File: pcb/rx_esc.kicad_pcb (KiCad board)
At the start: 2 copper layers, 54 parts, among them CON1 AVR-ISP-6, J1 CONN_01X02, J2 CONN_01X02, J3 CONN_02X06, J4 CONN_01X03, J5 CONN_01X03, J6 CONN_01X02, J7 CONN_01X02, Q1 Q_NMOS_DGS, Q2 Q_NMOS_DGS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

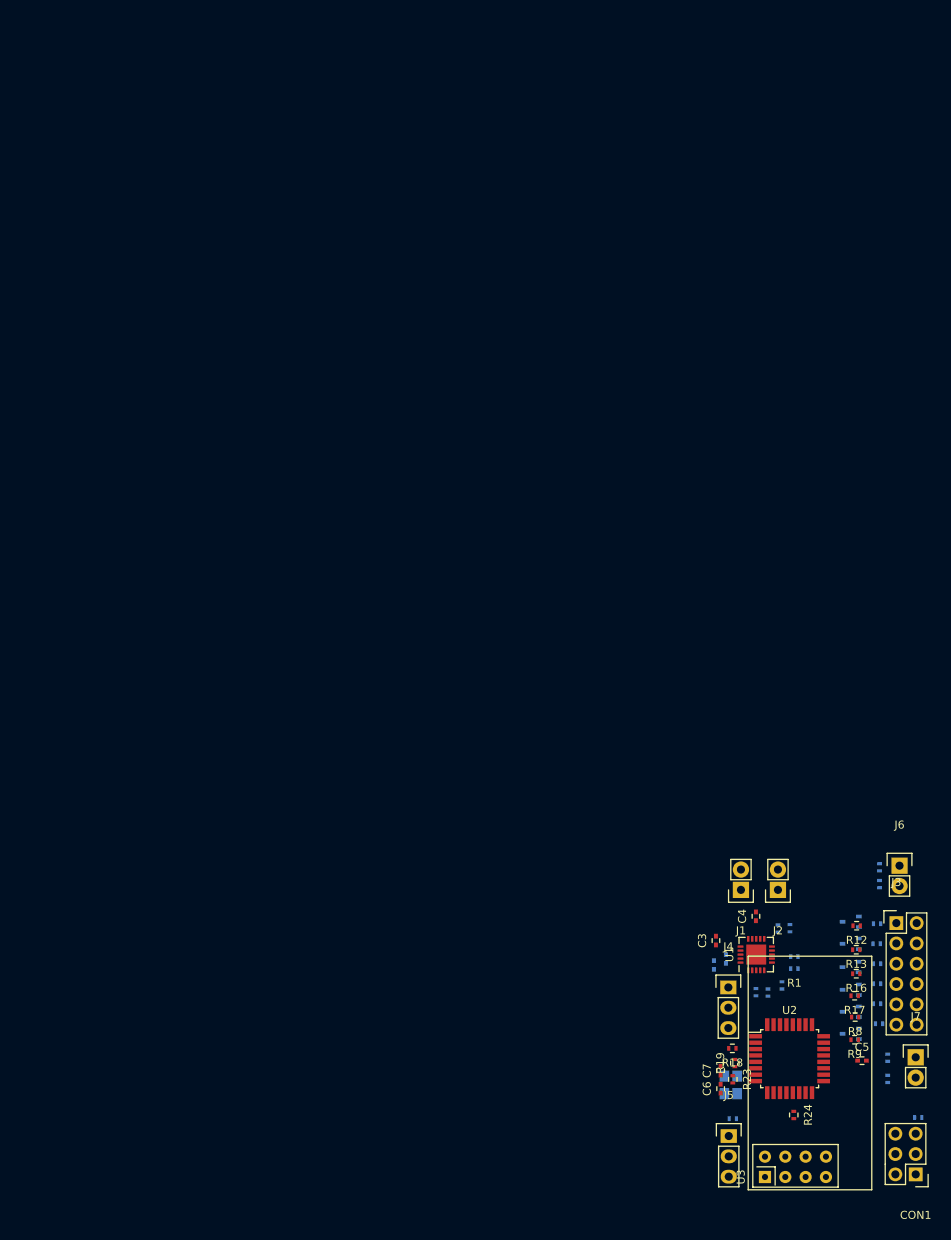
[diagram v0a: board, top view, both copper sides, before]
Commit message: VE 24-12-17 Add power supply
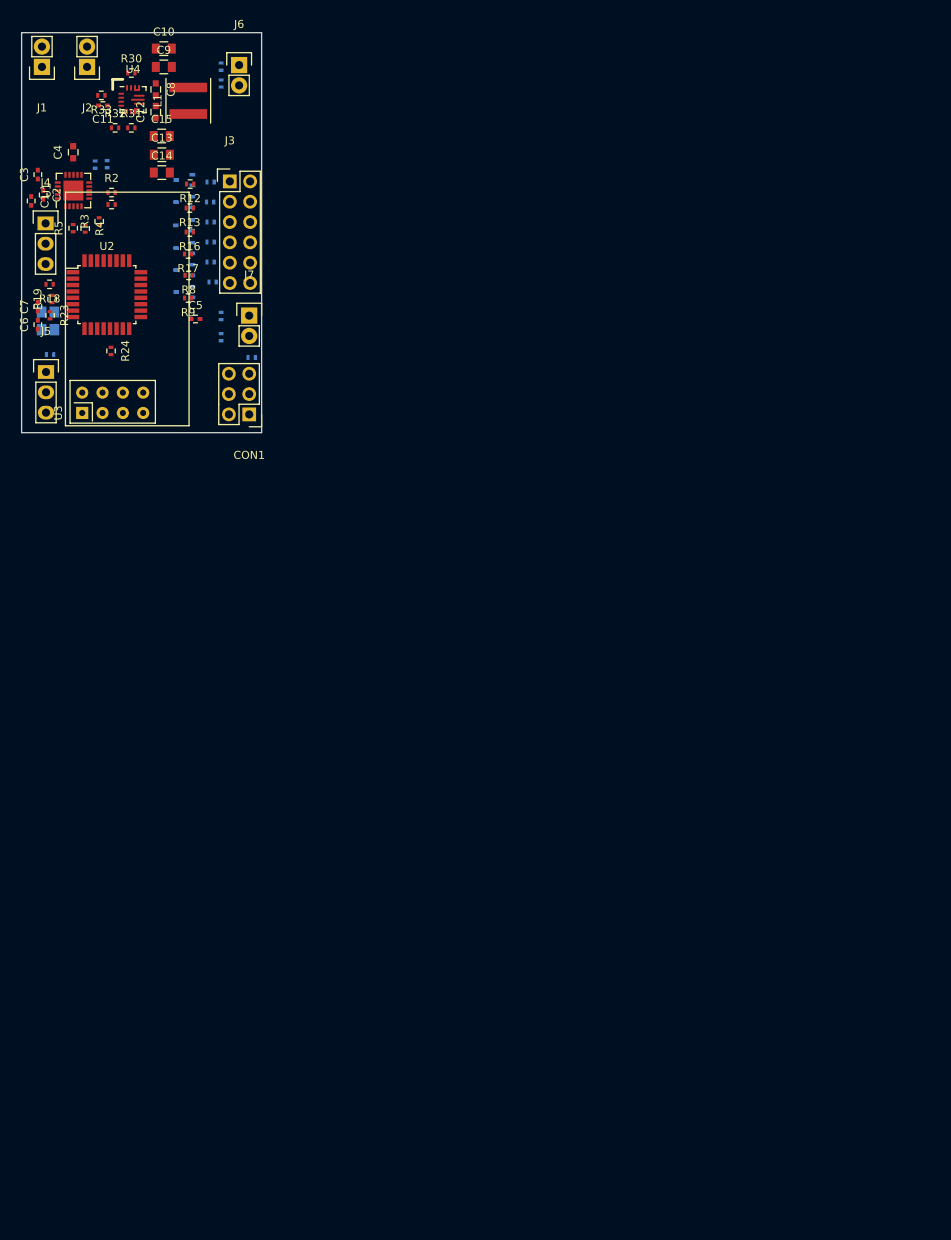
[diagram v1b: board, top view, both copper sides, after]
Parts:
- added C10: 10uf, Capacitors_SMD:C_0805, F.Cu at (17.8, -48.0)
- added C11: 100nF, Capacitors_SMD:C_0402, F.Cu at (10.2, -40.9)
- added C12: 10uf, Capacitors_SMD:C_0603, F.Cu at (16.8, -40.1)
- added C13: 10uf, Capacitors_SMD:C_0805, F.Cu at (17.5, -34.7)
- added C14: 10uf, Capacitors_SMD:C_0805, F.Cu at (17.5, -32.5)
- added C15: 10uf, Capacitors_SMD:C_0805, F.Cu at (17.5, -37.1)
- added C8: 10uf, Capacitors_SMD:C_0603, F.Cu at (16.8, -42.9)
- added C9: 10uf, Capacitors_SMD:C_0805, F.Cu at (17.8, -45.7)
- added L1: 1.5uH, Inductors_SMD:L_Coilcraft_XAL5030, F.Cu at (20.8, -41.5)
- added R30: 10k, Resistors_SMD:R_0402, F.Cu at (13.7, -45.0)
- added R31: 150k, Resistors_SMD:R_0402, F.Cu at (13.7, -38.1)
- added R32: 470k, Resistors_SMD:R_0402, F.Cu at (11.7, -38.1)
- added R33: 100k, Resistors_SMD:R_0402, F.Cu at (9.96, -42.2)
- added U4: TPS63070, FOOTPRINT:QFN-16-1EP_3x3mm_Pitch0.5mm, F.Cu at (13.9, -41.6)
- C1, C2, R1, R2, R3, R4, R5: moved to F.Cu
- C4: footprint Capacitors_SMD:C_0402 -> Capacitors_SMD:C_0603
- moved J1 135.0 mm to (2.54, -45.7)
- moved J2 134.3 mm to (8.18, -45.7)
- moved J6 129.7 mm to (27.2, -46.0)
- moved R28 129.6 mm to (24.9, -45.8)
- moved R29 129.6 mm to (24.9, -43.6)
- moved C1 128.1 mm to (1.20, -29.0)
- moved C2 128.1 mm to (2.70, -29.7)
- moved C4 128.1 mm to (6.45, -35.1)
- moved C6 128.1 mm to (2.03, -13.5)
- moved C7 128.1 mm to (2.03, -15.7)
- moved J4 128.1 mm to (3.00, -26.2)
- moved J5 128.1 mm to (3.05, -7.58)
- moved R1 128.1 mm to (11.2, -28.5)
- moved R18 128.1 mm to (3.50, -18.5)
- moved R19 128.1 mm to (3.81, -16.7)
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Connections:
- net Net-(C1-Pad1) renamed /CP1
- net Net-(C1-Pad2) renamed /CP2
- net Net-(C2-Pad1) renamed /CP3
- net Net-(C2-Pad2) renamed /CP4
- net Net-(C3-Pad1) renamed /VCP
- net Net-(C5-Pad1) renamed /AREF
- net Net-(J4-Pad1) renamed /SERVO1_OUT
- net Net-(J5-Pad1) renamed /SERVO2_OUT
- net Net-(J7-Pad1) renamed /AN
- net Net-(Q1-Pad1) renamed /OUT5_
- net Net-(Q1-Pad2) renamed /PD5_
- net Net-(Q2-Pad1) renamed /OUT6_
- net Net-(Q2-Pad2) renamed /PD6_
- net Net-(Q3-Pad1) renamed /OUT1_
- net Net-(Q3-Pad2) renamed /PC2_
- net Net-(Q4-Pad1) renamed /OUT2_
- net Net-(Q4-Pad2) renamed /PC3_
- net Net-(Q5-Pad1) renamed /OUT3_
- net Net-(Q5-Pad2) renamed /PC4_
- net Net-(Q6-Pad1) renamed /OUT4_
- net Net-(Q6-Pad2) renamed /PC5_
- net Net-(R1-Pad1) renamed /IN3_
- net Net-(R18-Pad1) renamed /PE0
- net Net-(R19-Pad1) renamed /PE1
- net Net-(R2-Pad1) renamed /IN4_
- net Net-(R5-Pad1) renamed /SLP
- net Net-(R6-Pad1) renamed /FL1
- net Net-(R7-Pad1) renamed /FL2
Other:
- board outline added: 30 x 50 mm

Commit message: VE 25-12-17 PCB routed schematic updated
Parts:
- C1, C2: footprint Capacitors_SMD:C_0402 -> Capacitors_SMD:C_0603
- Q1, Q2, Q3, Q4, Q5, Q6: value Q_NMOS_DGS -> MMBT2222
- R1, R2, R3, R4: footprint Resistors_SMD:R_0402 -> Resistors_SMD:R_0603
- R25, R26, R27: moved to F.Cu
- moved R25 8.94 mm to (12.5, -9.59), turned to 270 degrees
- moved J6 1.37 mm to (27.2, -44.6)
- moved R28 1.37 mm to (24.9, -44.4)
- moved R29 1.37 mm to (24.9, -42.3)
- moved J2 1.33 mm to (7.47, -44.6)
- moved C15 1.14 mm to (16.5, -36.6)
- moved C14 1.14 mm to (16.5, -32.0)
- moved C13 1.14 mm to (16.5, -34.2)
- moved J1 1.12 mm to (2.64, -44.6)
- moved R3 1.07 mm to (8.64, -26.3), turned to 180 degrees
- moved C10 1.05 mm to (16.8, -47.8)
- moved C9 1.02 mm to (16.8, -45.7)
- moved R4 0.96 mm to (8.64, -24.8), turned to 180 degrees
- moved R24 0.63 mm to (11.1, -9.60)
- turned R5 to 270 degrees
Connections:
- Q1 pad 1: /OUT5_ -> /PD4_
- Q1 pad 2: /PD5_ -> GND
- Q1 pad 3: GND -> /OUT5_
- Q2 pad 1: /OUT6_ -> /PD6_
- Q2 pad 2: /PD6_ -> GND
- Q2 pad 3: GND -> /OUT6_
- Q3 pad 1: /OUT1_ -> /PC5_
- Q3 pad 2: /PC2_ -> GND
- Q3 pad 3: GND -> /OUT1_
- Q4 pad 1: /OUT2_ -> /PC4_
- Q4 pad 2: /PC3_ -> GND
- Q4 pad 3: GND -> /OUT2_
- Q5 pad 1: /OUT3_ -> /PC3_
- Q5 pad 2: /PC4_ -> GND
- Q5 pad 3: GND -> /OUT3_
- Q6 pad 1: /OUT4_ -> /PC2_
- Q6 pad 2: /PC5_ -> GND
- Q6 pad 3: GND -> /OUT4_
- R12 pad 1: /PC2_ -> /PC5_
- R12 pad 2: /PC2 -> /PC5
- R13 pad 1: /PC3_ -> /PC4_
- R13 pad 2: /PC3 -> /PC4
- R16 pad 1: /PC4_ -> /PC3_
- R16 pad 2: /PC4 -> /PC3
- R17 pad 1: /PC5_ -> /PC2_
- R17 pad 2: /PC5 -> /PC2
- R8 pad 1: /PD5_ -> /PD4_
- R8 pad 2: /PD5 -> /PD4
- U2 pad 2: /CE -> /PD4
- U2 pad 23: /ADC_BATT -> /ADC_IN
- U2 pad 24: /ADC_IN -> /ADC_BATT
- U2 pad 9: /PD5 -> /CE
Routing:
- net GND: track 0.00 -> 175.7 mm, vias 0 -> 55
- net VCC: track 0.00 -> 160.3 mm, vias 0 -> 3
- net +BATT: track 0.00 -> 114.3 mm, vias 0 -> 6
- net /SCK: track 0.00 -> 33.5 mm
- net /SERVO1_OUT: track 0.00 -> 30.2 mm, vias 0 -> 1
- net /ADC_BATT: track 0.00 -> 29.5 mm, vias 0 -> 1
- net /RST: track 0.00 -> 28.4 mm, vias 0 -> 2
- net /MISO: track 0.00 -> 25.7 mm
- net /MOSI: track 0.00 -> 23.9 mm
- net /PD6: track 0.00 -> 18.2 mm, vias 0 -> 2
- net /PD4: track 0.00 -> 18.2 mm, vias 0 -> 2
- net /OUT2B: track 0.00 -> 17.4 mm
- net /OUT1B: track 0.00 -> 17.1 mm
- net /OUT1A: track 0.00 -> 15.5 mm
- net /OUT2A: track 0.00 -> 14.4 mm
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- added copper zone on F.Cu, net +BATT
- added copper zone on B.Cu, net GND
- added copper zone on F.Cu, net GND
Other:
- board size 30 x 50 mm -> 30 x 49 mm
- net class Default: clearance 0.2 -> 0.15
- net class batt added: clearance 0.15, trace_width 1, via_dia 0.6, via_drill 0.4
- rule trace_clearance: 0.2 -> 0.15
- rule trace_min: 0.2 -> 0.15
- board text added: "+ -"
- board text added: "1 2 3 4 5 6"
- board text added: "BAT"
- board text added: "FINIST'RC"
- board text added: "ISP"
- board text added: "M1 M2"
- board text added: "S + -"
- board text added: "S1"
- board text added: "S2"
